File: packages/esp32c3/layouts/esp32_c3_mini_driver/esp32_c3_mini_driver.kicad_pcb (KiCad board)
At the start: 2 copper layers, 9 parts

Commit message: Rebuild all
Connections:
- C3 pad 1: output-1 -> output
- R1 pad 1: line-12 -> line-9
- R2 pad 1: line-9 -> line-10
- R3 pad 2: output-1 -> output
- U1 pad 3: output -> output-1
- U1 pad 4: output -> output-1
- U2 pad 12: line-7 -> line-5
- U2 pad 13: line-2 -> line-13
- U2 pad 16: line-5 -> line-4
- U2 pad 18: line-11 -> line
- U2 pad 19: line-10 -> line-11
- U2 pad 20: line-4 -> line-1
- U2 pad 21: line-6 -> line-7
- U2 pad 22: line-9 -> line-10
- U2 pad 23: output -> output-1
- U2 pad 26: line-13 -> line-6
- U2 pad 27: line-3 -> line-2
- U2 pad 30: line-1 -> line-8
- U2 pad 31: line-8 -> line-3
- U2 pad 5: line-12 -> line-9
- U2 pad 6: line -> line-12
- U2 pad 8: output-1 -> output
- U3 pad 3: output-1 -> output
- U3 pad 4: output-1 -> output
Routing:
- net output-1: track 10.1 -> 1.53 mm
- net output: track 1.53 -> 10.1 mm
- net line-10: track 0.00 -> 5.04 mm
- net line-12: track 2.67 -> 0.00 mm
- net line-9: track 5.04 -> 2.67 mm
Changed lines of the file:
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@@
     (net 1 "hv")
     (net 2 "ic.footprint.pins[27].net-net")
-    (net 3 "line-2")
+    (net 3 "line-13")
     (net 4 "ic.footprint.pins[16].net-net")
     (net 5 "ic.footprint.pins[17].net-net")
-    (net 6 "line-12")
-    (net 7 "line-9")
-    (net 8 "line-7")
+    (net 6 "line-9")
+    (net 7 "line-10")
+    (net 8 "line-5")
     (net 9 "ic.footprint.pins[52].net-net")
     (net 10 "ic.footprint.pins[33].net-net")
@@
     (net 13 "ic.footprint.pins[8].net-net")
     (net 14 "ic.footprint.pins[21].net-net")
-    (net 15 "line-1")
-    (net 16 "line-3")
+    (net 15 "line-8")
+    (net 16 "line-2")
     (net 17 "ic.footprint.pins[25].net-net")
-    (net 18 "line-10")
-    (net 19 "line-5")
+    (net 18 "line-11")
+    (net 19 "line-4")
     (net 20 "gnd")
     (net 21 "ic.footprint.pins[26].net-net")
-    (net 22 "line")
-    (net 23 "line-4")
-    (net 24 "line-8")
-    (net 25 "output")
-    (net 26 "line-11")
-    (net 27 "output-1")
-    (net 28 "line-6")
-    (net 29 "line-13")
+    (net 22 "line-12")
+    (net 23 "line-1")
+    (net 24 "line-3")
+    (net 25 "output-1")
+    (net 26 "line")
+    (net 27 "output")
+    (net 28 "line-7")
+    (net 29 "line-6")
     (net 30 "ic.footprint.pins[6].net-net")
     (net 31 "ic.footprint.pins[1].net-net")
@@
             (size 0.57 0.54)
             (layers "F.Cu" "F.Mask" "F.Paste")
-            (net 6 "line-12")
+            (net 6 "line-9")
         )
         (pad "2" smd rect
@@
             (size 0.57 0.54)
             (layers "F.Cu" "F.Mask" "F.Paste")
-            (net 27 "output-1")
+            (net 27 "output")
         )
         (embedded_fonts no)
@@
             (size 0.4 0.8)
             (layers "F.Cu" "F.Mask" "F.Paste")
-            (net 6 "line-12")
+            (net 6 "line-9")
         )
         (pad "6" smd rect
@@
             (size 0.4 0.8)
             (layers "F.Cu" "F.Mask" "F.Paste")
-            (net 22 "line")
+            (net 22 "line-12")
         )
         (pad "7" smd rect
@@
             (size 0.4 0.8)
             (layers "F.Cu" "F.Mask" "F.Paste")
-            (net 27 "output-1")
+            (net 27 "output")
         )
         (pad "9" smd rect
@@
             (size 0.4 0.8)
             (layers "F.Cu" "F.Mask" "F.Paste")
-            (net 8 "line-7")
+            (net 8 "line-5")
         )
         (pad "13" smd rect
@@
             (size 0.4 0.8)
             (layers "F.Cu" "F.Mask" "F.Paste")
-            (net 3 "line-2")
+            (net 3 "line-13")
         )
         (pad "14" smd rect
@@
             (size 0.4 0.8)
             (layers "F.Cu" "F.Mask" "F.Paste")
-            (net 19 "line-5")
+            (net 19 "line-4")
         )
         (pad "17" smd rect
@@
             (size 0.4 0.8)
             (layers "F.Cu" "F.Mask" "F.Paste")
-            (net 26 "line-11")
+            (net 26 "line")
         )
         (pad "19" smd rect
@@
             (size 0.4 0.8)
             (layers "F.Cu" "F.Mask" "F.Paste")
-            (net 18 "line-10")
+            (net 18 "line-11")
         )
         (pad "20" smd rect
@@
             (size 0.4 0.8)
             (layers "F.Cu" "F.Mask" "F.Paste")
-            (net 23 "line-4")
+            (net 23 "line-1")
         )
         (pad "21" smd rect
@@
             (size 0.4 0.8)
             (layers "F.Cu" "F.Mask" "F.Paste")
-            (net 28 "line-6")
+            (net 28 "line-7")
         )
         (pad "22" smd rect
@@
             (size 0.4 0.8)
             (layers "F.Cu" "F.Mask" "F.Paste")
-            (net 7 "line-9")
+            (net 7 "line-10")
         )
         (pad "23" smd rect
@@
             (size 0.4 0.8)
             (layers "F.Cu" "F.Mask" "F.Paste")
-            (net 25 "output")
+            (net 25 "output-1")
         )
         (pad "24" smd rect
@@
             (size 0.4 0.8)
             (layers "F.Cu" "F.Mask" "F.Paste")
-            (net 29 "line-13")
+            (net 29 "line-6")
         )
         (pad "27" smd rect
@@
             (size 0.4 0.8)
             (layers "F.Cu" "F.Mask" "F.Paste")
-            (net 16 "line-3")
+            (net 16 "line-2")
         )
         (pad "28" smd rect
@@
             (size 0.4 0.8)
             (layers "F.Cu" "F.Mask" "F.Paste")
-            (net 15 "line-1")
+            (net 15 "line-8")
         )
         (pad "31" smd rect
@@
             (size 0.4 0.8)
             (layers "F.Cu" "F.Mask" "F.Paste")
-            (net 24 "line-8")
+            (net 24 "line-3")
         )
         (pad "32" smd rect
@@
             (size 0.79 0.54)
             (layers "F.Cu" "F.Mask" "F.Paste")
-            (net 27 "output-1")
+            (net 27 "output")
         )
         (pad "2" smd rect
@@
             (size 0.57 0.54)
             (layers "F.Cu" "F.Mask" "F.Paste")
-            (net 7 "line-9")
+            (net 7 "line-10")
         )
         (pad "2" smd rect
@@
             (size 1.05 0.7)
             (layers "F.Cu" "F.Mask" "F.Paste")
-            (net 25 "output")
+            (net 25 "output-1")
         )
         (pad "4" smd rect
@@
             (size 1.05 0.7)
             (layers "F.Cu" "F.Mask" "F.Paste")
-            (net 25 "output")
+            (net 25 "output-1")
         )
         (embedded_fonts no)
@@
             (size 1.05 0.7)
             (layers "F.Cu" "F.Mask" "F.Paste")
-            (net 27 "output-1")
+            (net 27 "output")
         )
         (pad "4" smd rect
@@
             (size 1.05 0.7)
             (layers "F.Cu" "F.Mask" "F.Paste")
-            (net 27 "output-1")
+            (net 27 "output")
         )
         (embedded_fonts no)

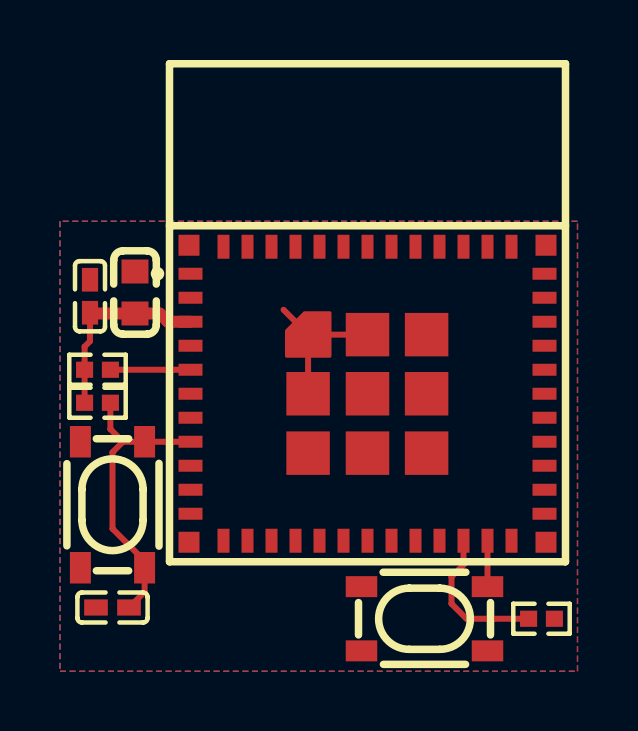
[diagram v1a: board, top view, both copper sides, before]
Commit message: Manually fix fp lib tables
fix some small bugs
fix package only modules (e.g. logos)
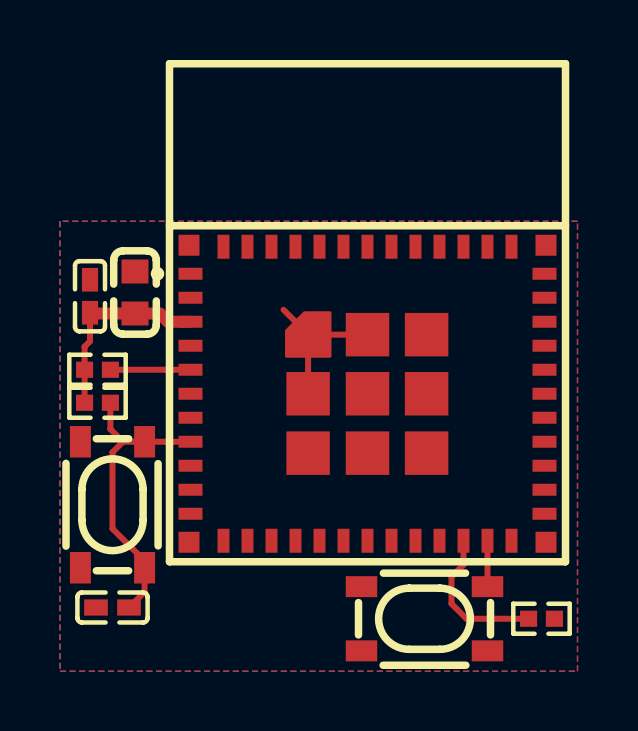
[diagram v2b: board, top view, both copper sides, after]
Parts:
- C1: footprint atopile:C0603-bd72f6 -> Samsung_Electro_Mechanics_CL10A226MQ8NRNC:C0603
- C2: footprint atopile:C0402-b3ef17 -> Samsung_Electro_Mechanics_CL05B104KO5NNNC:C0402
- C3: footprint atopile:C0402-b3ef17 -> Samsung_Electro_Mechanics_CL05A105KA5NQNC:C0402
- R1, R2, R3: footprint atopile:R0402-56259e -> UNI_ROYAL_0402WGF1002TCE:R0402
- U1, U3: footprint lib:KEY-SMD_4P-L4.2-W3.2-P2.20-LS4.6 -> ALPSALPINE_SKRPACE010:KEY-SMD_4P-L4.2-W3.2-P2.20-LS4.6
- U2: footprint atopile:WIFIM-SMD_ESP32-C3-MINI-1-fcb454 -> Espressif_Systems_ESP32_C3_MINI_1_N4:WIFIM-SMD_ESP32-C3-MINI-1
- turned U1 to 0 degrees
- turned U3 to -90 degrees
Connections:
- C3 pad 1: output -> line-14
- R1 pad 1: line-9 -> line-11
- R2 pad 1: line-10 -> line-1
- R3 pad 2: output -> line-14
- U1 pad 1: gnd -> line-2
- U1 pad 2: gnd -> line-2
- U1 pad 3: output-1 -> gnd
- U1 pad 4: output-1 -> gnd
- U2 pad 12: line-5 -> line-3
- U2 pad 13: line-13 -> line-7
- U2 pad 16: line-4 -> line-13
- U2 pad 18: line -> line-12
- U2 pad 19: line-11 -> line-15
- U2 pad 20: line-1 -> line-9
- U2 pad 21: line-7 -> line-8
- U2 pad 22: line-10 -> line-1
- U2 pad 23: output-1 -> line-2
- U2 pad 26: line-6 -> line
- U2 pad 27: line-2 -> line-5
- U2 pad 30: line-8 -> line-4
- U2 pad 31: line-3 -> line-6
- U2 pad 5: line-9 -> line-11
- U2 pad 6: line-12 -> line-10
- U2 pad 8: output -> line-14
- U3 pad 1: gnd -> line-14
- U3 pad 2: gnd -> line-14
- U3 pad 3: output -> gnd
- U3 pad 4: output -> gnd
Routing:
- net output: track 10.1 -> 0.00 mm
- net line-14: track 0.00 -> 10.1 mm
- net line-10: track 5.04 -> 0.00 mm
- net line-1: track 0.00 -> 5.04 mm
- net line-9: track 2.67 -> 0.00 mm
- net line-11: track 0.00 -> 2.67 mm
- net output-1: track 1.53 -> 0.00 mm
- net line-2: track 0.00 -> 1.53 mm

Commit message: Update 3D model locations
fix missing renders
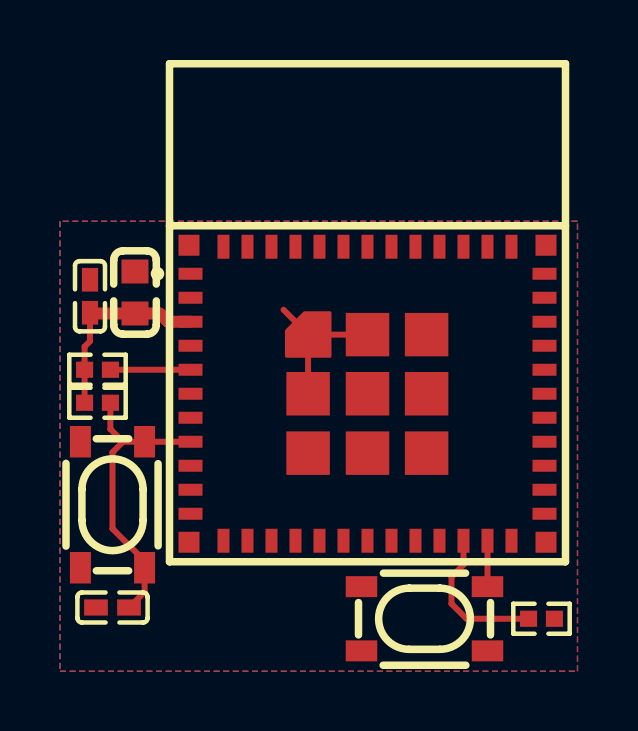
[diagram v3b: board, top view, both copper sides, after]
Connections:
- C3 pad 1: line-14 -> line
- R1 pad 1: line-11 -> line-13
- R2 pad 1: line-1 -> line-9
- R3 pad 2: line-14 -> line
- U1 pad 1: line-2 -> line-10
- U1 pad 2: line-2 -> line-10
- U2 pad 12: line-3 -> line-12
- U2 pad 13: line-7 -> line-1
- U2 pad 16: line-13 -> line-5
- U2 pad 18: line-12 -> line-14
- U2 pad 19: line-15 -> line-3
- U2 pad 20: line-9 -> line-15
- U2 pad 21: line-8 -> line-4
- U2 pad 22: line-1 -> line-9
- U2 pad 23: line-2 -> line-10
- U2 pad 26: line -> line-6
- U2 pad 27: line-5 -> line-8
- U2 pad 30: line-4 -> line-7
- U2 pad 31: line-6 -> line-11
- U2 pad 5: line-11 -> line-13
- U2 pad 6: line-10 -> line-2
- U2 pad 8: line-14 -> line
- U3 pad 1: line-14 -> line
- U3 pad 2: line-14 -> line
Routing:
- net line-14: track 10.1 -> 0.00 mm
- net line: track 0.00 -> 10.1 mm
- net line-9: track 0.00 -> 5.04 mm
- net line-1: track 5.04 -> 0.00 mm
- net line-13: track 0.00 -> 2.67 mm
- net line-11: track 2.67 -> 0.00 mm
- net line-2: track 1.53 -> 0.00 mm
- net line-10: track 0.00 -> 1.53 mm

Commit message: rebuild all packages & regenerate images of changed layouts (silk)
Add new scripts for version bump and build (based on atopile/packages)
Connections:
- C3 pad 1: line -> line-15
- R2 pad 1: line-9 -> line-7
- R3 pad 2: line -> line-15
- U1 pad 1: line-10 -> line-8
- U1 pad 2: line-10 -> line-8
- U2 pad 12: line-12 -> line
- U2 pad 16: line-5 -> line-2
- U2 pad 18: line-14 -> line-3
- U2 pad 19: line-3 -> line-4
- U2 pad 20: line-15 -> line-5
- U2 pad 21: line-4 -> line-6
- U2 pad 22: line-9 -> line-7
- U2 pad 23: line-10 -> line-8
- U2 pad 26: line-6 -> line-9
- U2 pad 27: line-8 -> line-10
- U2 pad 30: line-7 -> line-11
- U2 pad 31: line-11 -> line-12
- U2 pad 6: line-2 -> line-14
- U2 pad 8: line -> line-15
- U3 pad 1: line -> line-15
- U3 pad 2: line -> line-15
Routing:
- net line-15: track 0.00 -> 10.1 mm
- net line: track 10.1 -> 0.00 mm
- net line-9: track 5.04 -> 0.00 mm
- net line-7: track 0.00 -> 5.04 mm
- net line-8: track 0.00 -> 1.53 mm
- net line-10: track 1.53 -> 0.00 mm
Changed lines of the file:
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@@
     (net 5 "ic.footprint.pins[17].net-net")
     (net 6 "line-13")
-    (net 7 "line-9")
-    (net 8 "line-12")
+    (net 7 "line-7")
+    (net 8 "line")
     (net 9 "ic.footprint.pins[52].net-net")
     (net 10 "ic.footprint.pins[33].net-net")
@@
     (net 13 "ic.footprint.pins[8].net-net")
     (net 14 "ic.footprint.pins[21].net-net")
-    (net 15 "line-7")
-    (net 16 "line-8")
+    (net 15 "line-11")
+    (net 16 "line-10")
     (net 17 "ic.footprint.pins[25].net-net")
-    (net 18 "line-3")
-    (net 19 "line-5")
+    (net 18 "line-4")
+    (net 19 "line-2")
     (net 20 "gnd")
     (net 21 "ic.footprint.pins[26].net-net")
-    (net 22 "line-2")
-    (net 23 "line-15")
-    (net 24 "line-11")
-    (net 25 "line-14")
-    (net 26 "line-4")
-    (net 27 "line-6")
+    (net 22 "line-14")
+    (net 23 "line-5")
+    (net 24 "line-12")
+    (net 25 "line-3")
+    (net 26 "line-6")
+    (net 27 "line-9")
     (net 28 "ic.footprint.pins[6].net-net")
     (net 29 "ic.footprint.pins[1].net-net")
     (net 30 "ic.footprint.pins[28].net-net")
-    (net 31 "line")
-    (net 32 "line-10")
+    (net 31 "line-15")
+    (net 32 "line-8")
     (footprint "UNI_ROYAL_0402WGF1002TCE:R0402"
         (layer "F.Cu")
@@
             (size 0.57 0.54)
             (layers "F.Cu" "F.Mask" "F.Paste")
-            (net 31 "line")
+            (net 31 "line-15")
         )
         (embedded_fonts no)
@@
             (size 1.05 0.7)
             (layers "F.Cu" "F.Mask" "F.Paste")
-            (net 31 "line")
+            (net 31 "line-15")
         )
         (pad "2" smd rect
@@
             (size 1.05 0.7)
             (layers "F.Cu" "F.Mask" "F.Paste")
-            (net 31 "line")
+            (net 31 "line-15")
         )
         (pad "3" smd rect
@@
             (size 0.4 0.8)
             (layers "F.Cu" "F.Mask" "F.Paste")
-            (net 22 "line-2")
+            (net 22 "line-14")
         )
         (pad "7" smd rect
@@
             (size 0.4 0.8)
             (layers "F.Cu" "F.Mask" "F.Paste")
-            (net 31 "line")
+            (net 31 "line-15")
         )
         (pad "9" smd rect
@@
             (size 0.4 0.8)
             (layers "F.Cu" "F.Mask" "F.Paste")
-            (net 8 "line-12")
+            (net 8 "line")
         )
         (pad "13" smd rect
@@
             (size 0.4 0.8)
             (layers "F.Cu" "F.Mask" "F.Paste")
-            (net 19 "line-5")
+            (net 19 "line-2")
         )
         (pad "17" smd rect
@@
             (size 0.4 0.8)
             (layers "F.Cu" "F.Mask" "F.Paste")
-            (net 25 "line-14")
+            (net 25 "line-3")
         )
         (pad "19" smd rect
@@
             (size 0.4 0.8)
             (layers "F.Cu" "F.Mask" "F.Paste")
-            (net 18 "line-3")
+            (net 18 "line-4")
         )
         (pad "20" smd rect
@@
             (size 0.4 0.8)
             (layers "F.Cu" "F.Mask" "F.Paste")
-            (net 23 "line-15")
+            (net 23 "line-5")
         )
         (pad "21" smd rect
@@
             (size 0.4 0.8)
             (layers "F.Cu" "F.Mask" "F.Paste")
-            (net 26 "line-4")
+            (net 26 "line-6")
         )
         (pad "22" smd rect
@@
             (size 0.4 0.8)
             (layers "F.Cu" "F.Mask" "F.Paste")
-            (net 7 "line-9")
+            (net 7 "line-7")
         )
         (pad "23" smd rect
@@
             (size 0.4 0.8)
             (layers "F.Cu" "F.Mask" "F.Paste")
-            (net 32 "line-10")
+            (net 32 "line-8")
         )
         (pad "24" smd rect
@@
             (size 0.4 0.8)
             (layers "F.Cu" "F.Mask" "F.Paste")
-            (net 27 "line-6")
+            (net 27 "line-9")
         )
         (pad "27" smd rect
@@
             (size 0.4 0.8)
             (layers "F.Cu" "F.Mask" "F.Paste")
-            (net 16 "line-8")
+            (net 16 "line-10")
         )
         (pad "28" smd rect
@@
             (size 0.4 0.8)
             (layers "F.Cu" "F.Mask" "F.Paste")
-            (net 15 "line-7")
+            (net 15 "line-11")
         )
         (pad "31" smd rect
@@
             (size 0.4 0.8)
             (layers "F.Cu" "F.Mask" "F.Paste")
-            (net 24 "line-11")
+            (net 24 "line-12")
         )
         (pad "32" smd rect
@@
             (size 0.79 0.54)
             (layers "F.Cu" "F.Mask" "F.Paste")
-            (net 31 "line")
+            (net 31 "line-15")
         )
         (pad "2" smd rect
@@
             (size 0.57 0.54)
             (layers "F.Cu" "F.Mask" "F.Paste")
-            (net 7 "line-9")
+            (net 7 "line-7")
         )
         (pad "2" smd rect
@@
             (size 1.05 0.7)
             (layers "F.Cu" "F.Mask" "F.Paste")
-            (net 32 "line-10")
+            (net 32 "line-8")
         )
         (pad "2" smd rect
@@
             (size 1.05 0.7)
             (layers "F.Cu" "F.Mask" "F.Paste")
-            (net 32 "line-10")
+            (net 32 "line-8")
         )
         (pad "3" smd rect

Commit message: fix(esp32c3): frozen build & unconnected pads
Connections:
- net ic.footprint.pins[16].net-net renamed package.footprint.pins[16].net-net
- net ic.footprint.pins[17].net-net renamed package.footprint.pins[17].net-net
- net ic.footprint.pins[1].net-net renamed package.footprint.pins[1].net-net
- net ic.footprint.pins[20].net-net renamed package.footprint.pins[20].net-net
- net ic.footprint.pins[21].net-net renamed package.footprint.pins[21].net-net
- net ic.footprint.pins[25].net-net renamed package.footprint.pins[25].net-net
- net ic.footprint.pins[26].net-net renamed package.footprint.pins[26].net-net
- net ic.footprint.pins[27].net-net renamed package.footprint.pins[27].net-net
- net ic.footprint.pins[28].net-net renamed package.footprint.pins[28].net-net
- net ic.footprint.pins[33].net-net renamed package.footprint.pins[33].net-net
- net ic.footprint.pins[50].net-net renamed package.footprint.pins[50].net-net
- net ic.footprint.pins[52].net-net renamed package.footprint.pins[52].net-net
- net ic.footprint.pins[6].net-net renamed package.footprint.pins[6].net-net
- net ic.footprint.pins[8].net-net renamed package.footprint.pins[8].net-net
- net line-10 renamed IO19
- net line-13 renamed IO2
- net line-14 renamed IO3
- net line-15 renamed EN
- net line-8 renamed IO9
- net line-9 renamed IO18
- R2 pad 1: line-7 -> line
- U2 pad 12: line -> IO0
- U2 pad 13: line-1 -> IO1
- U2 pad 16: line-2 -> line-1
- U2 pad 18: line-3 -> line-4
- U2 pad 19: line-4 -> line-5
- U2 pad 20: line-5 -> line-6
- U2 pad 21: line-6 -> line-7
- U2 pad 22: line-7 -> line
- U2 pad 30: line-11 -> line-2
- U2 pad 31: line-12 -> line-3
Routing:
- net line-7: track 5.04 -> 0.00 mm
- net line: track 0.00 -> 5.04 mm
